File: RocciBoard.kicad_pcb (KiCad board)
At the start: 2 copper layers, 99 x 54 mm, 202 parts, among them J1 Battery, J10 M3, J11 I2C6, J12 Power, J13 M2, J14 I2C7, J2 I2C0, J3 I2C1, J4 I2C2, J5 I2C3, J6 M0, J7 I2C4, J8 M1, J9 I2C5, Q1 IRF7404, Q2 2N7002, U1 LMR33630, U10 LM317_TO-252, U11 CJ431, U12 CJ431, U2 LM317_TO-252, U3 LM317_TO-252, U4 TPS3700, U5 TCA9548A, U6 DRV8871, U7 DRV8871, U8 DRV8871, U9 DRV8871

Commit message: V 1.1
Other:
- board text added: "RocciBoard V1.1"
- board text removed: "RocciBoard V1.0"
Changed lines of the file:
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@@
     (effects (font (size 1 1) (thickness 0.15)) (justify left bottom mirror))
   )
-  (gr_text "RocciBoard V1.0" (at 153.67 97.536) (layer "B.SilkS")
+  (gr_text "RocciBoard V1.1" (at 153.67 97.536) (layer "B.SilkS")
     (effects (font (size 1 1) (thickness 0.15)) (justify left bottom mirror))
   )
@@
     (effects (font (size 1 1) (thickness 0.15)) (justify left bottom))
   )
-  (gr_text "RocciBoard V1.0" (at 199.878 126.024) (layer "F.SilkS")
+  (gr_text "RocciBoard V1.1" (at 199.878 126.024) (layer "F.SilkS")
     (effects (font (size 1 1) (thickness 0.15)) (justify left bottom))
   )

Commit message: fix #13 #12 #11 #10
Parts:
- added JP12: Jumper_2_Bridged, Jumper:SolderJumper-2_P1.3mm_Open_Pad1.0x1.5mm, B.Cu at (175.5, 93.5)
- added RESET: SW_DIP_x01, Button_Switch_SMD:SW_Push_1P1T_XKB_TS-1187A, F.Cu at (123.5, 82.1)
- added TP12: ~, TestPoint:TestPoint_Pad_D1.0mm, B.Cu at (138.4, 104.5)
- Q1: value IRF7404 -> IRF 7424
- moved TP7 26.0 mm to (164.7, 89.9)
- moved Q2 7.43 mm to (122.6, 92.1), turned to 0 degrees
- moved D17 2.49 mm to (125.1, 88.5), turned to 90 degrees
- moved R42 2.23 mm to (123.4, 88.6)
- moved R48 2.10 mm to (121.8, 88.6)
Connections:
- net Net-(U4-INB-) renamed SHUTOFF
- C14 pad 1: +12V -> +12VA
- C15 pad 1: +12V -> +12VA
- C16 pad 1: +12V -> +12VA
- C17 pad 1: +12V -> +12VA
- C18 pad 1: +12V -> +12VA
- C8 pad 1: +12V -> /12V_after_fuse
- D32 pad 3: +12V -> /12V_after_fuse
- F2 pad 2: +12V -> /12V_after_fuse
- Q1 pad 1: +12V -> /12V_after_fuse
- Q1 pad 2: +12V -> /12V_after_fuse
- Q1 pad 3: +12V -> /12V_after_fuse
- R13 pad 1: +12V -> /12V_after_fuse
- R14 pad 1: +12V -> /12V_after_fuse
- TP7 pad 1: +12V -> /12V_after_fuse
- U4 pad 5: +12V -> /12V_after_fuse
- U6 pad 5: +12V -> +12VA
- U7 pad 5: +12V -> +12VA
- U8 pad 5: +12V -> +12VA
- U9 pad 5: +12V -> +12VA
- XA1 pad RST1: unconnected-(XA1-RESET-PadRST1) -> Net-(XA1-RESET)
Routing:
- net Net-(XA1-RESET): track 0.00 -> 84.5 mm
- net +12VA: track 156.3 -> 174.1 mm, vias 7 -> 44
- net +12V: track 15.5 -> 0.00 mm, vias 37 -> 0
- net /12V_after_fuse: track 0.00 -> 13.2 mm, vias 0 -> 1
- net SHUTOFF: track 5.29 -> 16.1 mm
- net ERROR_LED: track 30.7 -> 35.4 mm
- net +5V: track 293.3 -> 290.5 mm
- net Net-(Q2-D): track 4.03 -> 5.00 mm
- net Net-(U8-ILIM): track 8.89 -> 8.06 mm
- net Net-(D17-K): track 2.43 -> 1.68 mm
- net Net-(D33-G): track 24.4 -> 24.9 mm
- net /_8V: vias 0 -> 1
- added copper zone on B.Cu, net +12VA
- added copper zone on F.Cu, net /12V_after_fuse
- removed copper zone on B.Cu, net +12V
- removed copper zone on F.Cu, net +12V
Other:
- board text removed: "Battery"

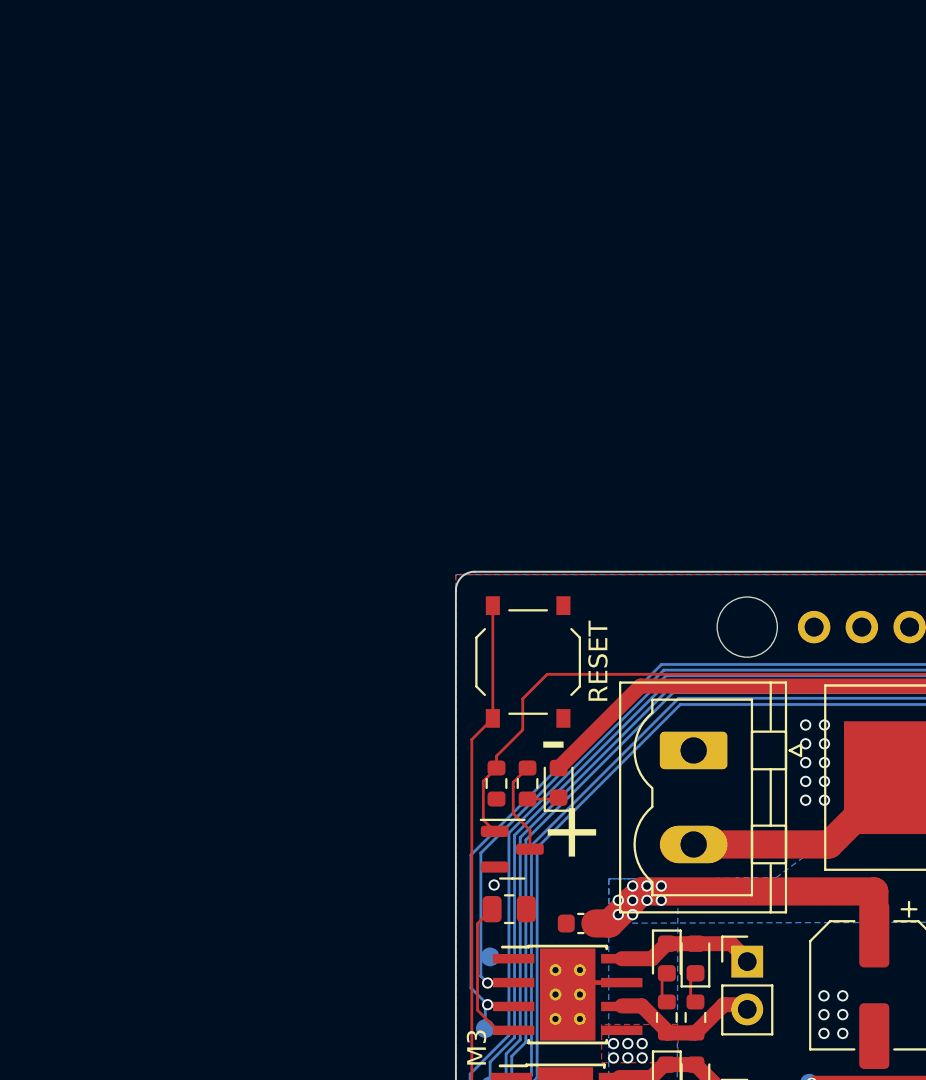
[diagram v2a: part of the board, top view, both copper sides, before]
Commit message: add xt60 and spereate i2c pwr and data jumper
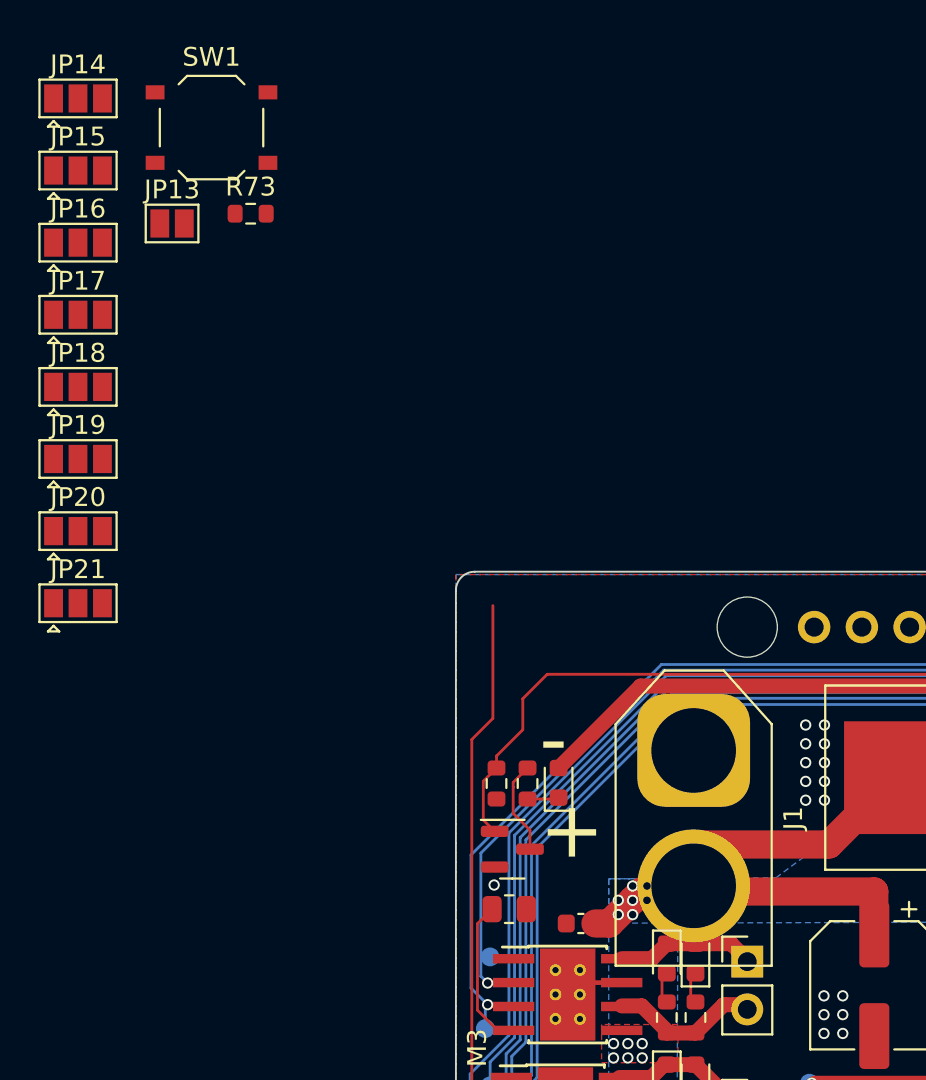
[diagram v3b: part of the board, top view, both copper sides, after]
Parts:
- removed RESET: SW_DIP_x01, Button_Switch_SMD:SW_Push_1P1T_XKB_TS-1187A
- added JP13: Jumper_2_Open, Jumper:SolderJumper-2_P1.3mm_Open_Pad1.0x1.5mm, F.Cu at (104.5, 58.8)
- added JP14: I2C0_PWR, Jumper:SolderJumper-3_P1.3mm_Open_Pad1.0x1.5mm, F.Cu at (99.5, 52.1)
- added JP15: I2C1_PWR, Jumper:SolderJumper-3_P1.3mm_Open_Pad1.0x1.5mm, F.Cu at (99.5, 56.0)
- added JP16: I2C2_PWR, Jumper:SolderJumper-3_P1.3mm_Open_Pad1.0x1.5mm, F.Cu at (99.5, 59.8)
- added JP17: I2C3_PWR, Jumper:SolderJumper-3_P1.3mm_Open_Pad1.0x1.5mm, F.Cu at (99.5, 63.7)
- added JP18: I2C4_PWR, Jumper:SolderJumper-3_P1.3mm_Open_Pad1.0x1.5mm, F.Cu at (99.5, 67.5)
- added JP19: I2C6_PWR, Jumper:SolderJumper-3_P1.3mm_Open_Pad1.0x1.5mm, F.Cu at (99.5, 71.3)
- added JP20: I2C5_PWR, Jumper:SolderJumper-3_P1.3mm_Open_Pad1.0x1.5mm, F.Cu at (99.5, 75.2)
- added JP21: I2C7_PWR, Jumper:SolderJumper-3_P1.3mm_Open_Pad1.0x1.5mm, F.Cu at (99.5, 79.0)
- added R73: 9100k 1%, Resistor_SMD:R_0603_1608Metric, F.Cu at (108.7, 58.3)
- added SW1: SW_DIP_x01, Button_Switch_SMD:SW_Push_1P1T_XKB_TS-1187A, F.Cu at (106.6, 53.7)
- J1: footprint Connector_Phoenix_MSTB:PhoenixContact_MSTBVA_2,5_2-G_1x02_P5.00mm_Vertical -> Connector_AMASS:AMASS_XT60-M_1x02_P7.20mm_Vertical
- JP1: value I2C0_VCC -> I2C0_VDD
- JP10: value I2C6_VCC -> I2C6_VDD
- JP11: value I2C7_VCC -> I2C7_VDD
- JP2: value I2C1_VCC -> I2C1_VDD
- JP3: value I2C2_VCC -> I2C2_VDD
- JP4: value I2C3_VCC -> I2C3_VDD
- JP8: value I2C4_VCC -> I2C4_VDD
- JP9: value I2C5_VCC -> I2C5_VDD
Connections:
- F1 pad 1: Net-(JP1-C) -> Net-(JP14-C)
- F10 pad 1: Net-(JP11-C) -> Net-(JP21-C)
- F3 pad 1: Net-(JP2-C) -> Net-(JP15-C)
- F4 pad 1: Net-(JP3-C) -> Net-(JP16-C)
- F5 pad 1: Net-(JP4-C) -> Net-(JP17-C)
- F6 pad 1: Net-(JP8-C) -> Net-(JP18-C)
- F7 pad 1: Net-(JP9-C) -> Net-(JP20-C)
- F8 pad 1: Net-(JP10-C) -> Net-(JP19-C)

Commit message: more progress with nxt shield
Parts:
- JP13, JP14, JP15, JP16, JP17, JP18, JP19, JP20, JP21: moved to B.Cu
- moved JP14 105.8 mm to (191.6, 104.3), turned to -90 degrees
- moved JP21 101.6 mm to (191.6, 122.0), turned to -90 degrees
- moved JP19 100.7 mm to (186.6, 122.0), turned to -90 degrees
- moved JP15 99.6 mm to (186.6, 104.3), turned to -90 degrees
- moved JP20 94.5 mm to (181.6, 122.0), turned to -90 degrees
- moved JP18 94.4 mm to (176.6, 122.0), turned to -90 degrees
- moved JP16 93.3 mm to (181.6, 104.3), turned to -90 degrees
- moved R73 87.2 mm to (189.1, 92.0), turned to -90 degrees
- moved JP17 87.1 mm to (176.6, 104.3), turned to -90 degrees
- moved JP13 86.7 mm to (184.6, 92.1), turned to 90 degrees
- moved SW1 33.0 mm to (123.5, 82.1), turned to -90 degrees
- moved JP12 6.74 mm to (182.1, 92.1), turned to -90 degrees
- moved TP9 6.09 mm to (195.1, 110.3)
- moved TP8 6.07 mm to (195.1, 108.3)
- moved JP8 4.91 mm to (174.1, 122.0), turned to -90 degrees
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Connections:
- net Net-(JP14-C) renamed /VCC_UF_I2C0
- net Net-(JP15-C) renamed /VCC_UF_I2C1
- net Net-(JP16-C) renamed /VCC_UF_I2C2
- net Net-(JP17-C) renamed /VCC_UF_I2C3
- net Net-(JP18-C) renamed /VCC_UF_I2C4
- net Net-(JP19-C) renamed /VCC_UF_I2C6
- net Net-(JP20-C) renamed /VCC_UF_I2C5
- net Net-(JP21-C) renamed /VCC_UF_I2C7
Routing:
- net /VCC_I2C0: track 72.2 -> 36.3 mm, vias 1 -> 0
- net +3V3: track 121.9 -> 91.2 mm
- net /VCC_I2C1: track 59.0 -> 31.8 mm, vias 1 -> 0
- net /VCC_I2C7: track 43.7 -> 16.6 mm, vias 1 -> 0
- net /VCC_I2C3: track 39.9 -> 13.1 mm, vias 1 -> 0
- net /VCC_I2C2: track 48.4 -> 28.2 mm, vias 1 -> 0
- net /VCC_I2C5: track 24.9 -> 5.18 mm, vias 1 -> 0
- net /VCC_I2C6: track 33.7 -> 17.3 mm, vias 1 -> 0
- net /VCC_I2C4: track 18.5 -> 3.98 mm, vias 1 -> 0
- net Net-(JP3-C): track 13.8 -> 1.50 mm, vias 1 -> 0
- net +5V: track 290.5 -> 279.1 mm, vias 16 -> 10
- net Net-(JP4-C): track 13.2 -> 1.93 mm, vias 1 -> 0
- net /VCC_UF_I2C3: track 0.00 -> 7.02 mm, vias 0 -> 1
- net /VCC_UF_I2C0: track 0.00 -> 6.80 mm, vias 0 -> 1
- net SHUTOFF: track 16.1 -> 9.51 mm
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
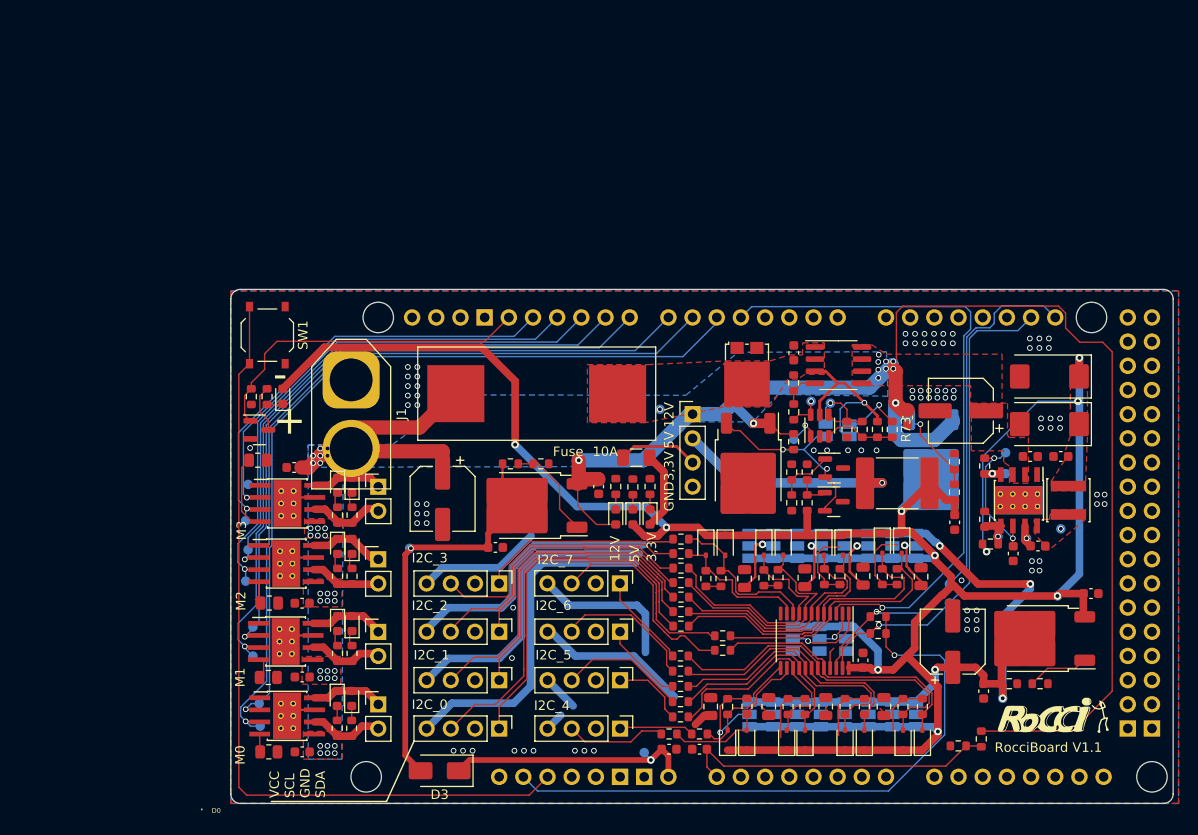
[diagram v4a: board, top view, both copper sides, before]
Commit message: update rocci board to have XT60 and more jumper
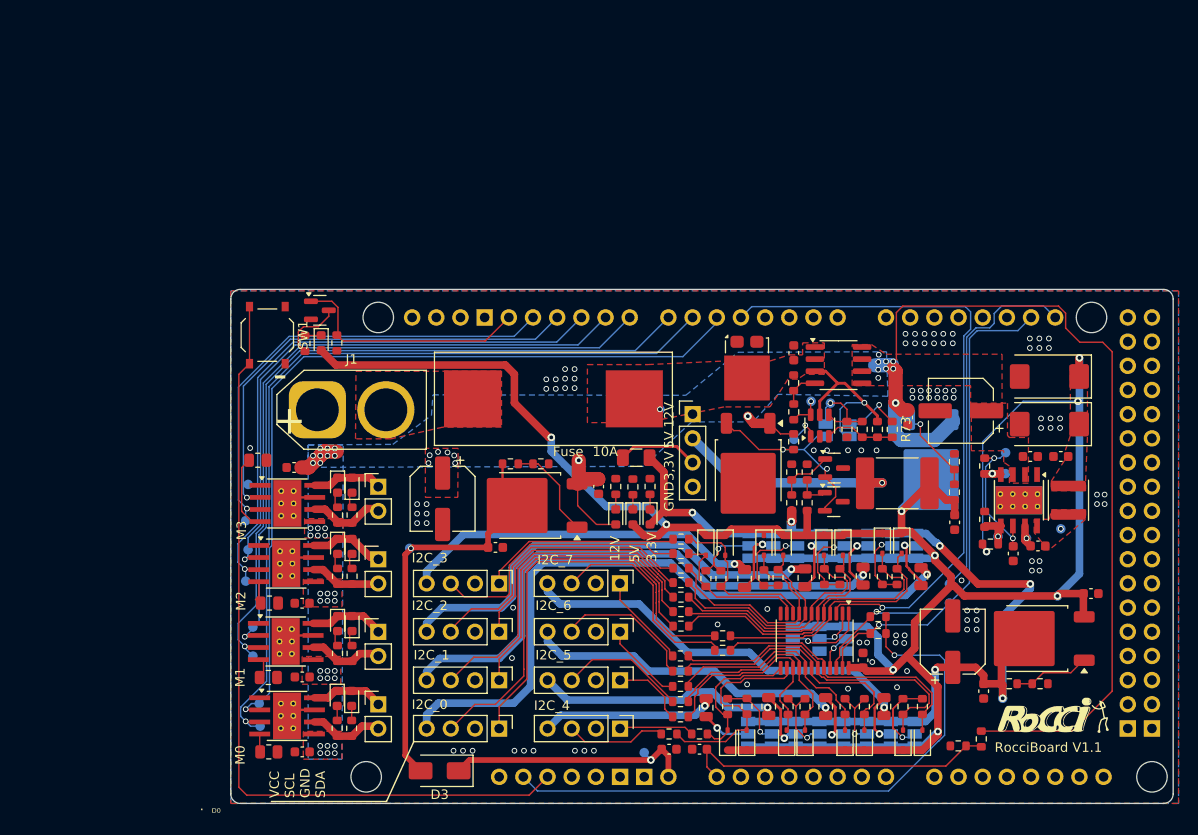
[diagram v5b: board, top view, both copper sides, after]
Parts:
- moved Q2 14.1 mm to (129.0, 79.5)
- moved R48 10.6 mm to (130.8, 82.9)
- moved D17 6.92 mm to (129.1, 82.9), turned to -90 degrees
- moved R42 6.87 mm to (127.4, 83.0), turned to -90 degrees
- moved J1 4.74 mm to (128.7, 90.0), turned to 0 degrees
- moved JP18 3.35 mm to (174.0, 124.0)
- moved JP19 3.35 mm to (184.0, 124.0)
- moved JP20 3.35 mm to (179.0, 124.0)
- moved JP21 3.35 mm to (189.0, 124.0)
- moved JP10 3.12 mm to (186.5, 124.0)
- moved JP11 3.12 mm to (191.5, 124.0)
- moved JP8 3.12 mm to (176.5, 124.0)
- moved JP9 3.12 mm to (181.5, 124.0)
- moved U2 2.00 mm to (204.3, 114.0)
- moved U3 1.93 mm to (151.0, 100.0)
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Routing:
- net +12VA: track 174.5 -> 123.2 mm, vias 44 -> 50
- net /VCC_I2C0: track 36.3 -> 70.8 mm, vias 0 -> 1
- net /VCC_I2C1: track 31.8 -> 58.5 mm, vias 0 -> 1
- net /VCC_I2C7: track 16.6 -> 43.0 mm, vias 0 -> 1
- net /VCC_I2C3: track 13.1 -> 37.8 mm, vias 0 -> 1
- net /VCC_I2C5: track 5.18 -> 25.9 mm, vias 0 -> 1
- net /VCC_I2C2: track 28.2 -> 47.1 mm, vias 0 -> 1
- net /VCC_I2C6: track 17.3 -> 34.3 mm, vias 0 -> 1
- net /VCC_I2C4: track 3.98 -> 18.3 mm, vias 0 -> 1
- net /12V_input: track 12.6 -> 0.00 mm
- net +3V3: track 91.2 -> 102.5 mm, vias 4 -> 6
- net ERROR_LED: track 35.4 -> 25.2 mm
- net Net-(JP3-C): track 1.50 -> 9.65 mm, vias 0 -> 1
- net /VCC_UF_I2C5: track 0.00 -> 6.32 mm, vias 0 -> 1
- net Net-(D15-A): track 17.0 -> 22.8 mm
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- added copper zone on F.Cu, net /12V_input

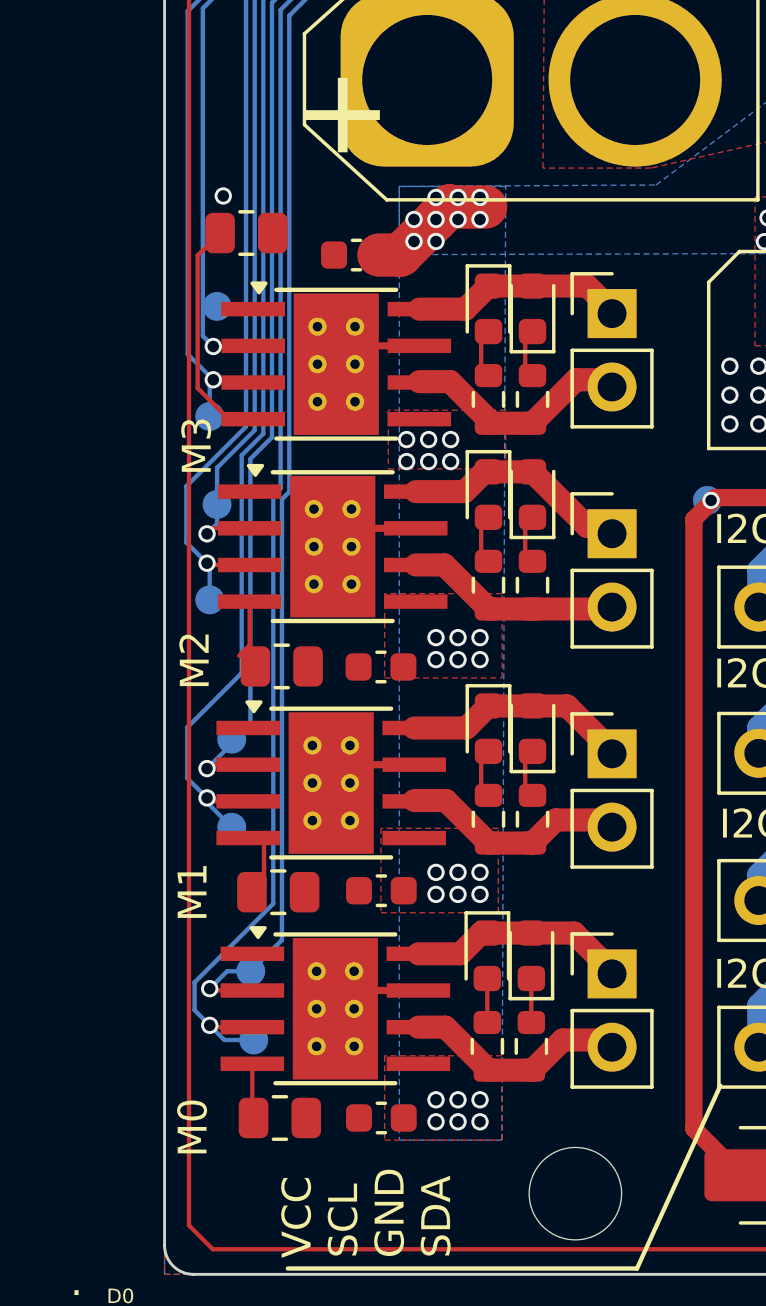
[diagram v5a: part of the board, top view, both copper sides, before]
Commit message: update rocciboard with thermal release
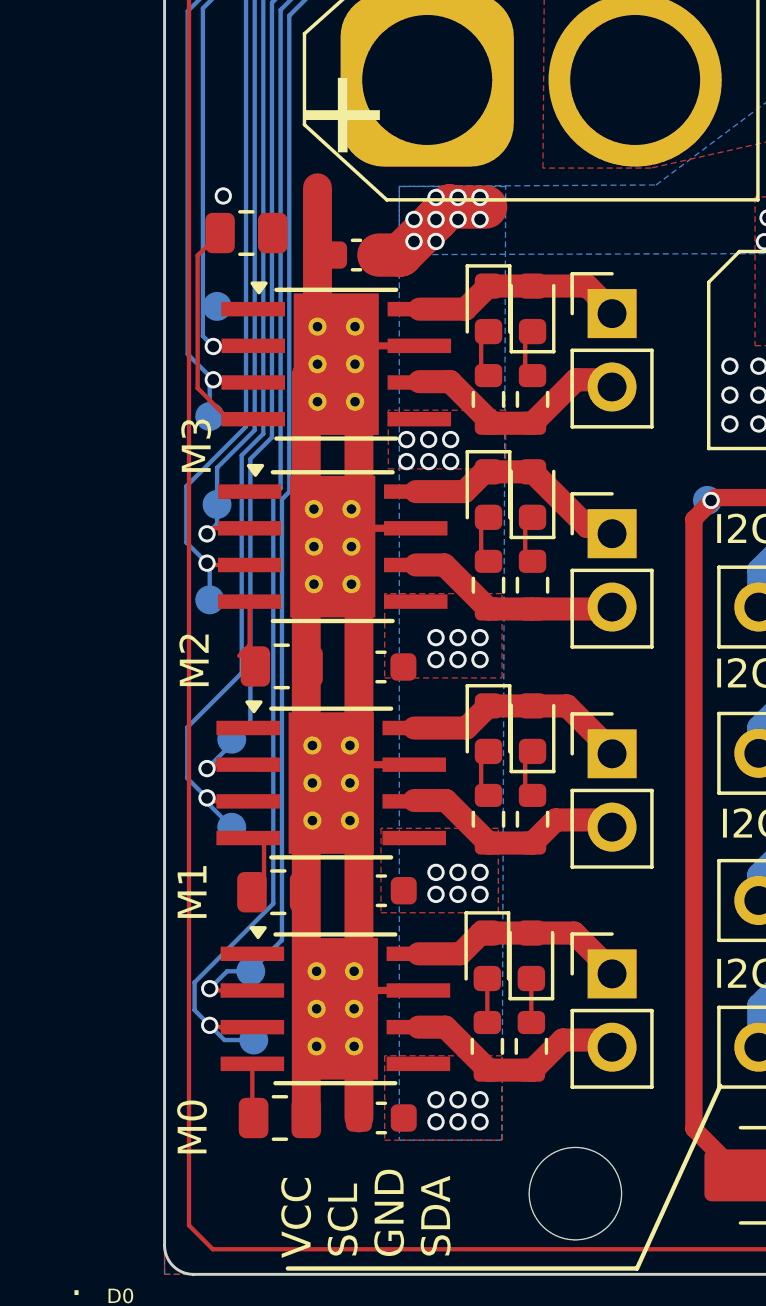
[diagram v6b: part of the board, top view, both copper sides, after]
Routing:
- net GND: track 6.36 -> 64.9 mm
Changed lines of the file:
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@@
 			(pinfunction "Pin_1")
 			(pintype "passive")
+			(thermal_bridge_width 2)
+			(thermal_gap 0.2)
 		)
 		(pad "2" thru_hole circle
@@
 			(layers "F.Paste")
 			(roundrect_rratio 0.090909)
+			(thermal_bridge_width 2)
+			(thermal_gap 0.2)
 		)
 		(pad "" smd roundrect
@@
 			(pinfunction "A2")
 			(pintype "passive")
+			(thermal_bridge_width 2)
+			(thermal_gap 0.2)
 		)
 		(pad "3" smd roundrect
@@
 	)
 	(segment
+		(start 124.929 98.5045)
+		(end 124.929 93.695)
+		(width 1)
+		(layer "F.Cu")
+		(net 1)
+	)
+	(segment
+		(start 124.5405 125.904)
+		(end 124.5405 100.193)
+		(width 1)
+		(layer "F.Cu")
+		(net 1)
+	)
+	(segment
+		(start 126.365 98.6405)
+		(end 126.229 98.5045)
+		(width 1)
+		(layer "F.Cu")
+		(net 1)
+	)
+	(segment
 		(start 128.423 121.489)
 		(end 126.833 121.489)
@@
 	)
 	(segment
+		(start 126.365 125.904)
+		(end 126.365 98.6405)
+		(width 1)
+		(layer "F.Cu")
+		(net 1)
+	)
+	(segment
 		(start 128.331 105.4865)
 		(end 126.741 105.4865)
@@
 	)
 	(segment
+		(start 124.5405 100.193)
+		(end 124.929 99.8045)
+		(width 1)
+		(layer "F.Cu")
+		(net 1)
+	)
+	(segment
 		(start 128.454 99.1695)
 		(end 126.864 99.1695)
@@
 		(hatch edge 0.5)
 		(priority 11)
-		(connect_pads yes
+		(connect_pads
 			(clearance 0.2)
 		)
@@
 		(filled_areas_thickness no)
 		(fill yes
-			(thermal_gap 0.5)
-			(thermal_bridge_width 0.5)
+			(thermal_gap 0.2)
+			(thermal_bridge_width 2)
 		)
 		(polygon
@@
 		(hatch edge 0.5)
 		(priority 5)
-		(connect_pads yes
+		(connect_pads
 			(clearance 0.2)
 		)
@@
 		(filled_areas_thickness no)
 		(fill yes
-			(thermal_gap 0.5)
-			(thermal_bridge_width 0.5)
+			(thermal_gap 0.2)
+			(thermal_bridge_width 2)
 		)
 		(polygon
@@
 		(layer "F.Cu")
 		(hatch edge 0.5)
-		(connect_pads yes
+		(connect_pads
 			(clearance 0.2)
 		)
